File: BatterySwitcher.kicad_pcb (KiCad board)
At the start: 2 copper layers, 18.5 x 5 mm, 5 parts, among them J1 53047-0210, J2 M22-2510146, J3 M22-2510146

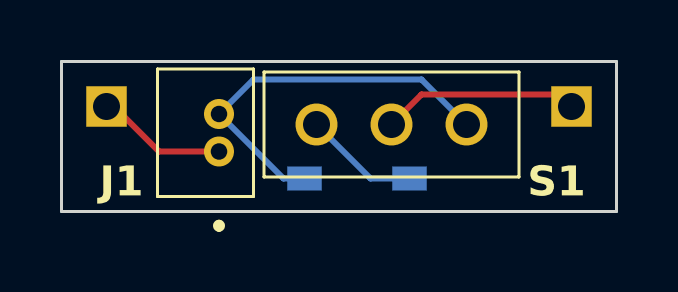
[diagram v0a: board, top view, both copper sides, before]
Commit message: changed battery connector to be placed on the back
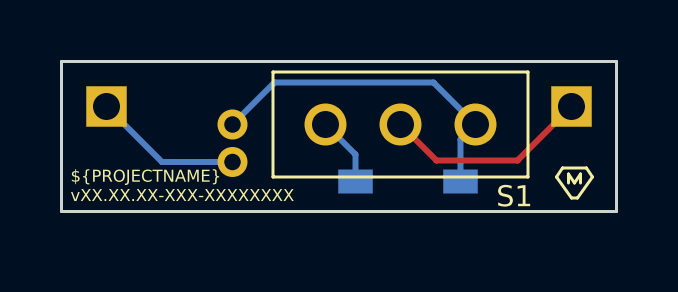
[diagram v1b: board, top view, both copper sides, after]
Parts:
- J1: moved to B.Cu
- moved D1 1.70 mm to (151.1, 65.0), turned to 180 degrees
- moved J1 0.57 mm to (145.2, 64.3)
- moved S1 0.30 mm to (150.8, 63.1)
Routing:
- net Battery  +: track 13.1 -> 11.4 mm
- net Net-(D1-A): track 3.85 -> 2.31 mm
- net Battery  -: track 4.37 -> 4.97 mm

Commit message: fix(publish release): using mathieudutour/github-tag-action in release.yml
Now the tag info is retrieved by a dry run of the mathieudutour/github-tag-action that not creates any tag in the end term

The version placeholder has been shorten too
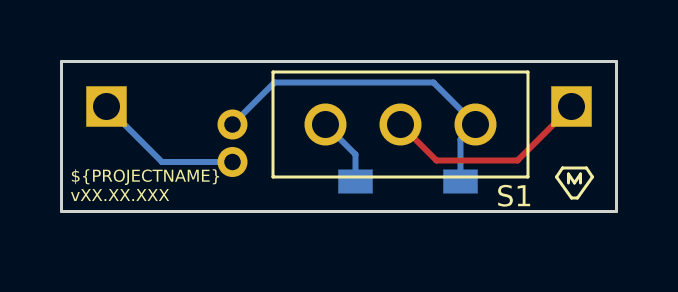
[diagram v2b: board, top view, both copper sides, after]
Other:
- board text added: "${PROJECTNAME} vXX.XX.XXX"
- board text removed: "${PROJECTNAME} vXX.XX.XX-XXX-XXXXXXXX"
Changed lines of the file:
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@@
 		(layer "Edge.Cuts")
 	)
-	(gr_text "${PROJECTNAME}\nvXX.XX.XX-XXX-XXXXXXXX"
+	(gr_text "${PROJECTNAME}\nvXX.XX.XXX"
 		(at 139.8 65.7 0)
 		(layer "F.SilkS")
